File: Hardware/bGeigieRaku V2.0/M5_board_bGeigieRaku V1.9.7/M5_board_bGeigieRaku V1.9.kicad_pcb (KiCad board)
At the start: 2 copper layers, 129.4 x 64.6 mm, 29 parts, among them J1 M5 2x15 pin, J10 QI GND, J11 QI charger Plus, J2 Geiger, J3 GPS, J4 Geiger 2, J5 Extra support header, J7 Conn_01x14_Female, J8 QI charger GND, J9 QI Plus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

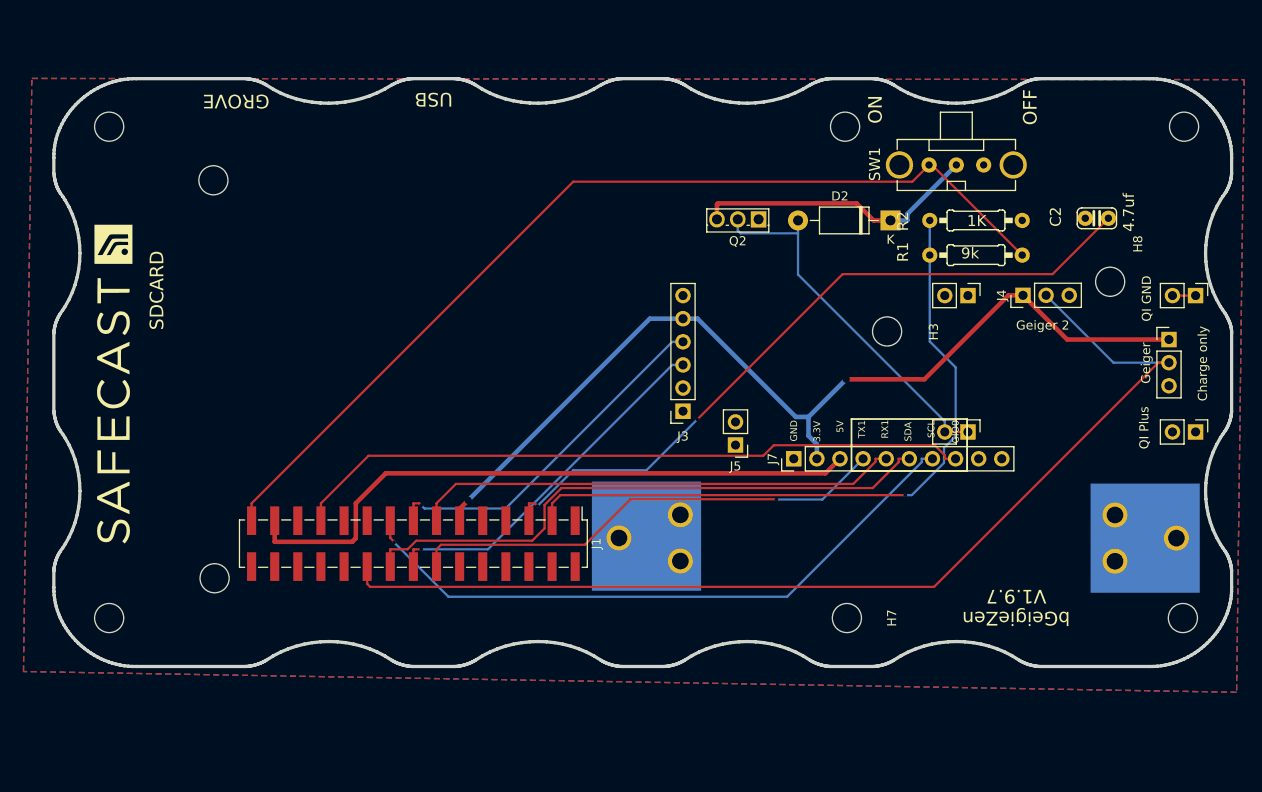
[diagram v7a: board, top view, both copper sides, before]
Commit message: V1.9.8 hardware and LiPo and charger changes
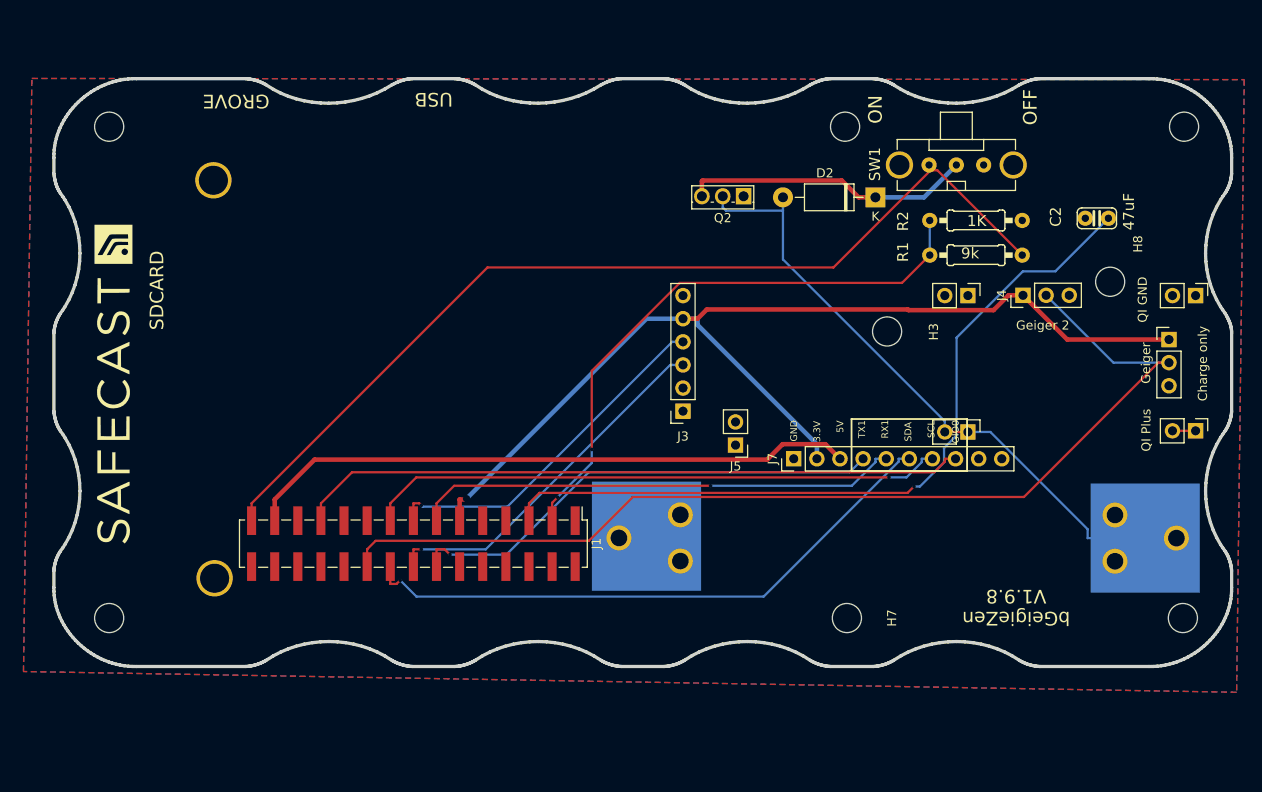
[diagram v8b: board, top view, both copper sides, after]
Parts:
- C2: value 4.7uf -> 47uF
- moved J10 15.0 mm to (210.0, 90.5)
- moved J9 14.9 mm to (210.0, 105.4)
- moved D2 3.03 mm to (174.9, 79.7)
- moved Q2 3.03 mm to (160.4, 79.6)
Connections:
- D2 pad 2: Net-(J11-Pad1) -> Net-(BT1-Pad1)
- J11 pad 1: Net-(J11-Pad1) -> Net-(BT1-Pad1)
- J11 pad 2: Net-(J11-Pad1) -> Net-(BT1-Pad1)
- Q2 pad 2: Net-(J11-Pad1) -> Net-(BT1-Pad1)
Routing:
- net Net-(BT1-Pad1): track 3.43 -> 72.0 mm
- net Net-(J11-Pad1): track 40.4 -> 0.00 mm
- net Net-(J1-Pad3): track 75.2 -> 64.5 mm, vias 1 -> 2
- net 3.3V: track 104.9 -> 114.1 mm, vias 2 -> 1
- net /Reset: track 78.8 -> 85.8 mm, vias 2 -> 1
- net /SCL: track 70.7 -> 63.7 mm
- net 5V: track 70.5 -> 67.6 mm
- net /GIO2: track 116.9 -> 115.1 mm
- net /SDA: track 64.8 -> 66.3 mm, vias 0 -> 1
- net /GIO0: track 75.1 -> 73.8 mm
- net /RX1: track 53.5 -> 53.6 mm, vias 0 -> 1
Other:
- board text added: "NOTES: 2021-03-09 for V1.9.7 - check power track width - realign the holes for M5Stack mounts - check alignments all holes 2021-03-13 - pin headers for M5Stack are Hirosugi Instruments: PSM-4200233-15 - https://macsbug.wordpress.com/2018/08/19/low-cost-proto-module-of-m5stack-part-2/ 2021-03-16 - moved M5Stack connector y -2.0 mm - moved mounting holes M5Stack x -2.1 mm 2021-03-31 - SWITCHED qi C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"
- board text added: "bGeigieZen V1.9.8"
- board text removed: "NOTES: 2021-03-09 for V1.9.7 - check power track width - realign the holes for M5Stack mounts - check alignments all holes 2021-03-13 - pin headers for M5Stack are Hirosugi Instruments: PSM-4200233-15 - https://macsbug.wordpress.com/2018/08/19/low-cost-proto-module-of-m5stack-part-2/ 2021-03-16 - moved M5Stack connector y -2.0 mm - moved mounting holes M5Stack x -2.1 mm"
- board text removed: "bGeigieZen V1.9.7"
